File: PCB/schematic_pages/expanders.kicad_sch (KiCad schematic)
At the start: 32 parts

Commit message: repo rearrange
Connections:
- net I2C_SCL renamed I2C_SCK

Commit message: new schematics
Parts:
- removed B24, B25, B26: ~, symbol Symbols:Push_Switch
- added S1, S2, S3: ~, Footprints:MTS-102 Switch, symbol Symbols:Switch
- B1, B11, B12, B13, B14, B15, B16, B17, B18, B19, B2, B20, B21, B22, B23, B3, B4, B5, B6, B7, B8, B9: footprint (none) -> Footprints:Mechanical Switch
- B24: renamed from B27; footprint (none) -> Footprints:Mechanical Switch
- B25: renamed from B28; footprint (none) -> Footprints:Mechanical Switch
- B26: renamed from B29; footprint (none) -> Footprints:Mechanical Switch
- C42, C43: footprint (none) -> Footprints:0603_C
- EX1, EX2: footprint (none) -> Footprints:MCP23017 GPIO Expander
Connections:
- net GND: now also S1.3, S2.3, S3.3
- net at EX2.21 (GPA0): now also S2.2
- net at EX2.22 (GPA1): now also S3.2
- net at EX2.8 (GPB7): now also S1.2
- no-connect marks 0 -> 3

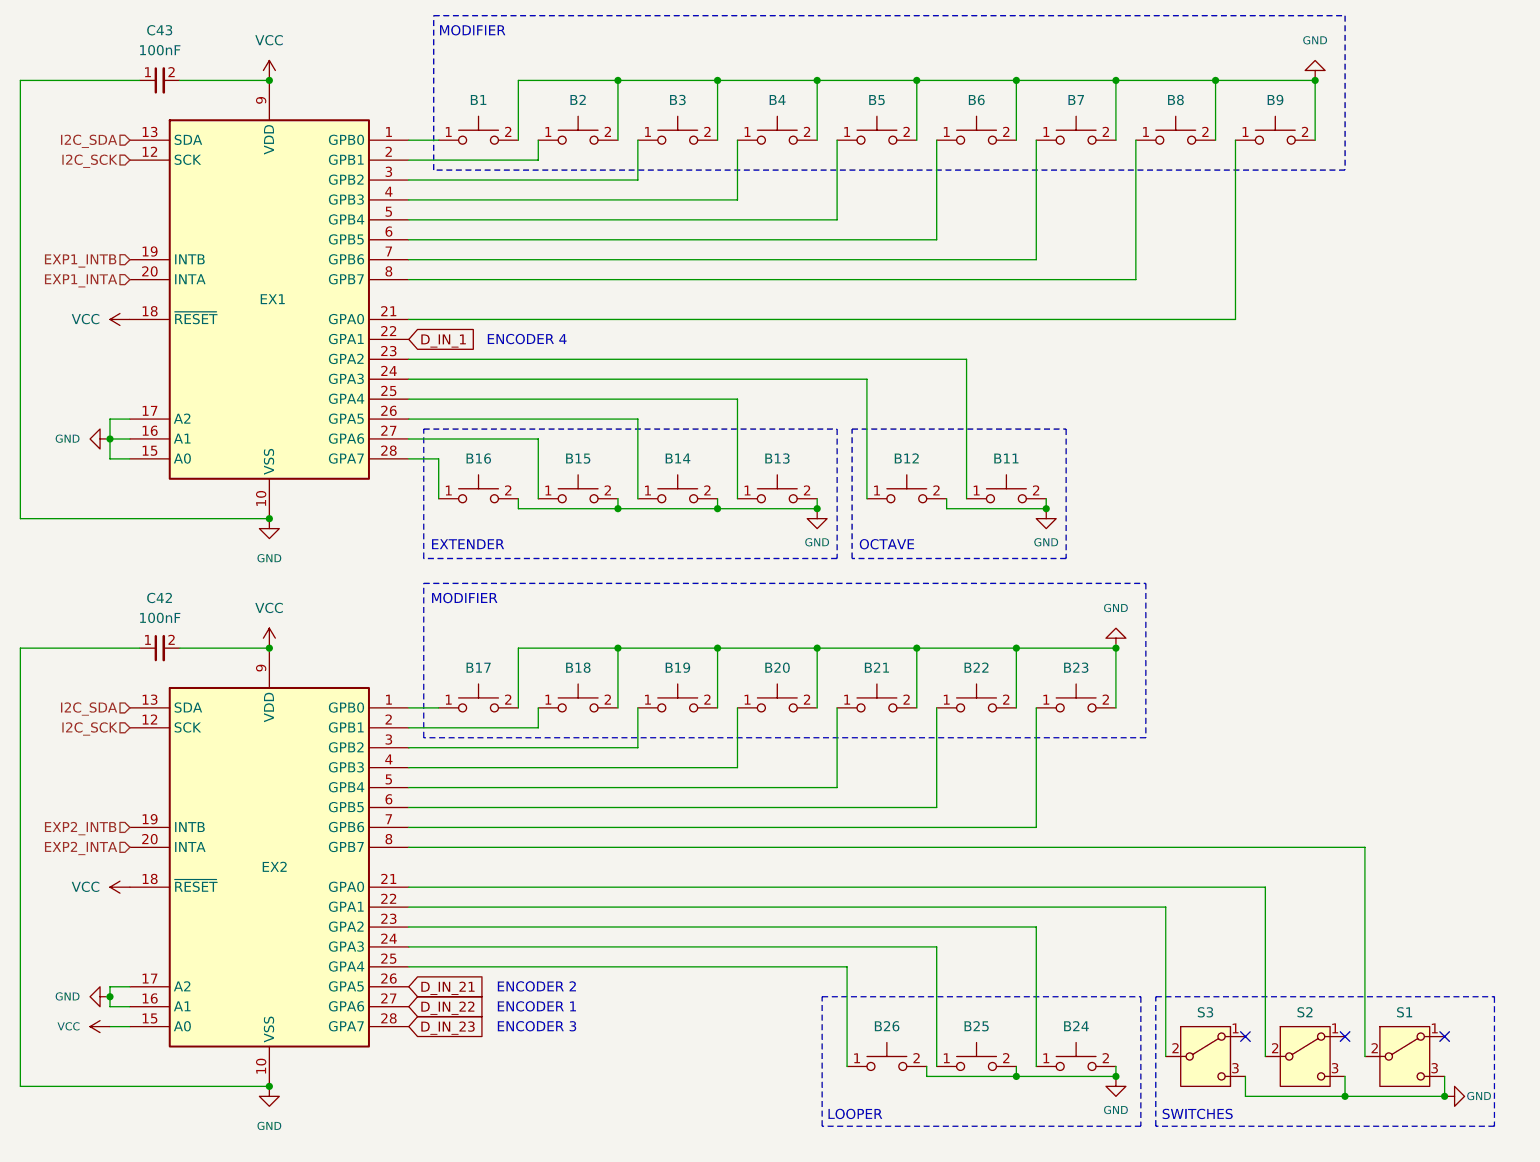
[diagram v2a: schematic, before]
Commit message: ISP ports, RESET lines, MIDI DIN 5
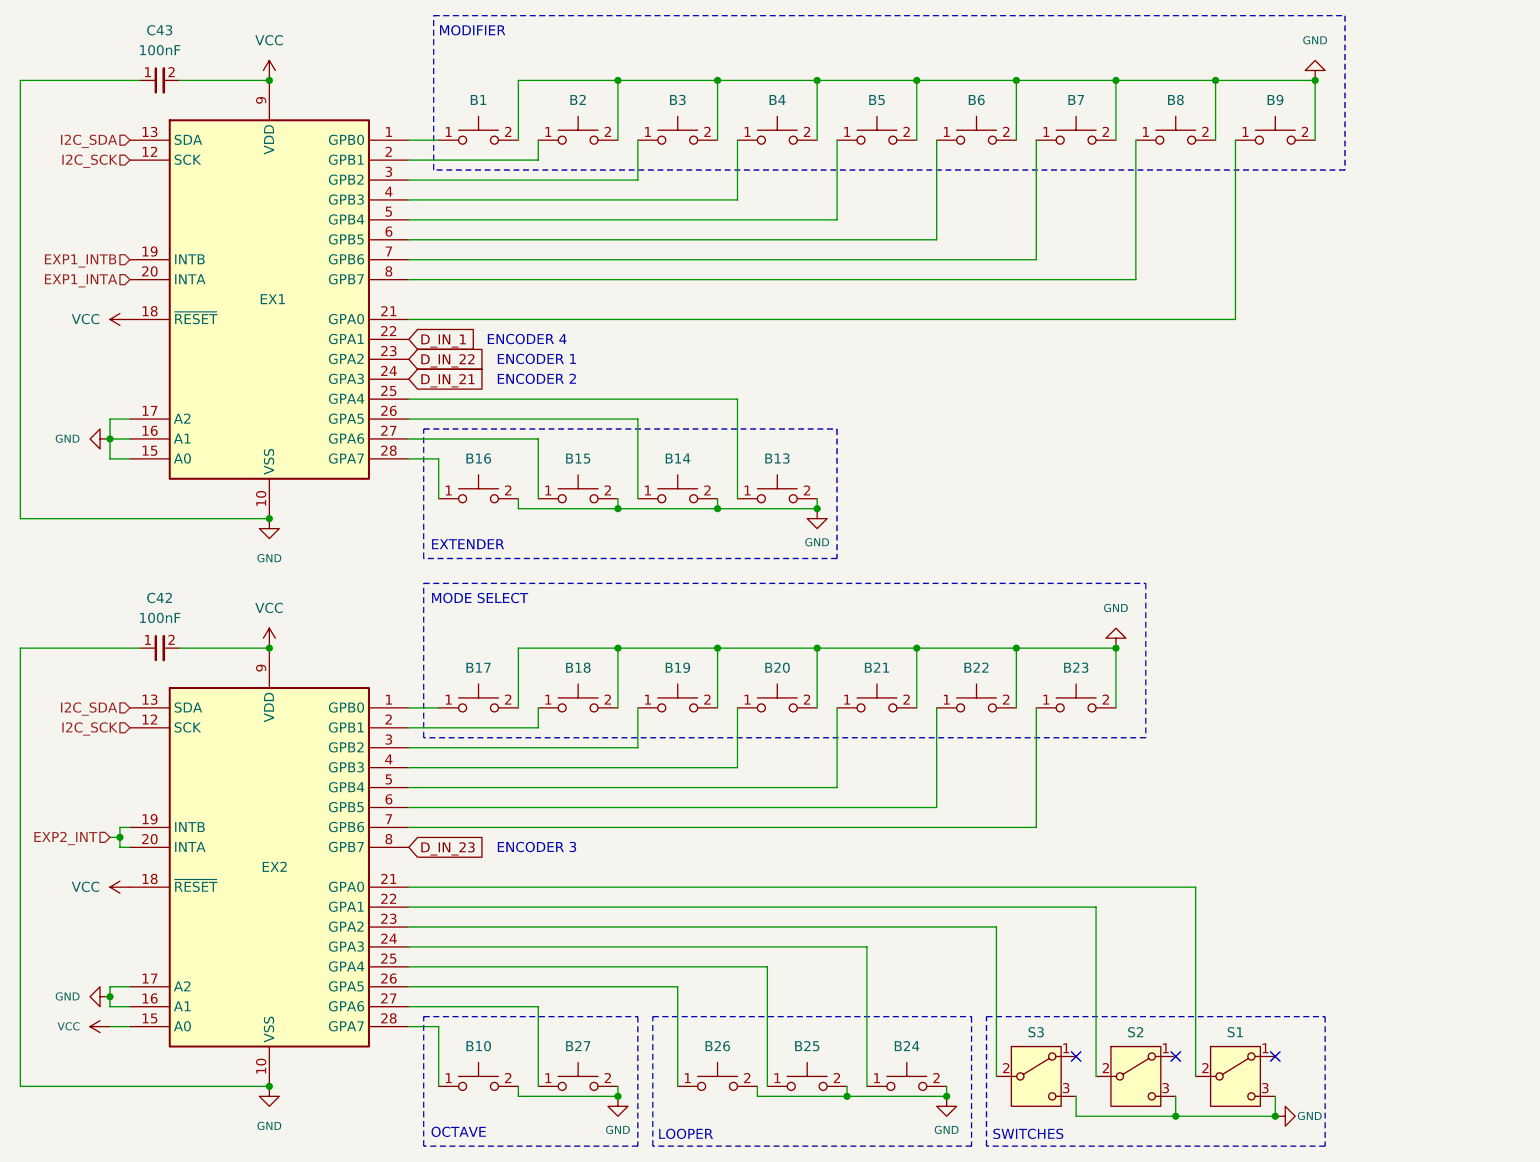
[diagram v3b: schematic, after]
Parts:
- removed B11, B12: ~, Footprints:Mechanical Switch, symbol Symbols:Push_Switch
- added B10, B27: ~, Footprints:Mechanical Switch, symbol Symbols:Push_Switch
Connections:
- net EXP2_INTB is gone; now on net EXP2_INT: EX2.19 (INTB)
- net D_IN_21: now also EX1.24 (GPA3); no longer EX2.26 (GPA5)
- net D_IN_22: now also EX1.23 (GPA2); no longer EX2.27 (GPA6)
- net D_IN_23: now also EX2.8 (GPB7); no longer EX2.28 (GPA7)
- net GND: now also B10.2, B27.2
- net at EX2.21 (GPA0): now also S1.2; no longer S2.2
- net at EX2.22 (GPA1): now also S2.2; no longer S3.2
- net at EX2.23 (GPA2): now also S3.2; no longer B24.1
- net at EX2.24 (GPA3): now also B24.1; no longer B25.1
- net at EX2.25 (GPA4): now also B25.1; no longer B26.1
- net EXP2_INTA renamed EXP2_INT
- new net: B26.1, EX2.26 (GPA5)
- new net: B27.1, EX2.27 (GPA6)
- new net: B10.1, EX2.28 (GPA7)
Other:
- note added: "MODE SELECT"
- moved on the sheet: B24, B25, B26, S1, S2, S3

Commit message: pcbing
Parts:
- renumbered B13 to B10, B14 to B11, B15 to B12, B16 to B13, B17 to B14, B18 to B15, B19 to B16, B20 to B17, B21 to B18, B22 to B19, B23 to B20, B24 to B21, B25 to B22, B26 to B23, B27 to B24, B10 to B25
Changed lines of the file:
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@@
 		(dnp no)
 		(fields_autoplaced yes)
-		(property "Reference" "B17"
+		(property "Reference" "B14"
 			(at 111.76 99.06 0)
 			(effects
@@
 			(project "MCU_328p"
 				(path "/de43e009-b04c-42c1-b131-cdc664039a0d/8f5845f6-f6f8-4f8f-ac6e-d033b6efee1b"
-					(reference "B17")
+					(reference "B14")
 					(unit 1)
 				)
@@
 		(dnp no)
 		(fields_autoplaced yes)
-		(property "Reference" "B25"
+		(property "Reference" "B22"
 			(at 153.67 147.32 0)
 			(effects
@@
 			(project "MCU_328p"
 				(path "/de43e009-b04c-42c1-b131-cdc664039a0d/8f5845f6-f6f8-4f8f-ac6e-d033b6efee1b"
-					(reference "B25")
+					(reference "B22")
 					(unit 1)
 				)
@@
 		(dnp no)
 		(fields_autoplaced yes)
-		(property "Reference" "B18"
+		(property "Reference" "B15"
 			(at 124.46 99.06 0)
 			(effects
@@
 			(project "MCU_328p"
 				(path "/de43e009-b04c-42c1-b131-cdc664039a0d/8f5845f6-f6f8-4f8f-ac6e-d033b6efee1b"
-					(reference "B18")
+					(reference "B15")
 					(unit 1)
 				)
@@
 		(dnp no)
 		(fields_autoplaced yes)
-		(property "Reference" "B10"
+		(property "Reference" "B25"
 			(at 111.76 147.32 0)
 			(effects
@@
 			(project "Harmora"
 				(path "/de43e009-b04c-42c1-b131-cdc664039a0d/8f5845f6-f6f8-4f8f-ac6e-d033b6efee1b"
-					(reference "B10")
+					(reference "B25")
 					(unit 1)
 				)
@@
 		(dnp no)
 		(fields_autoplaced yes)
-		(property "Reference" "B26"
+		(property "Reference" "B23"
 			(at 142.24 147.32 0)
 			(effects
@@
 			(project "MCU_328p"
 				(path "/de43e009-b04c-42c1-b131-cdc664039a0d/8f5845f6-f6f8-4f8f-ac6e-d033b6efee1b"
-					(reference "B26")
+					(reference "B23")
 					(unit 1)
 				)
@@
 		(dnp no)
 		(fields_autoplaced yes)
-		(property "Reference" "B23"
+		(property "Reference" "B20"
 			(at 187.96 99.06 0)
 			(effects
@@
 			(project "MCU_328p"
 				(path "/de43e009-b04c-42c1-b131-cdc664039a0d/8f5845f6-f6f8-4f8f-ac6e-d033b6efee1b"
-					(reference "B23")
+					(reference "B20")
 					(unit 1)
 				)
@@
 		(dnp no)
 		(fields_autoplaced yes)
-		(property "Reference" "B21"
+		(property "Reference" "B18"
 			(at 162.56 99.06 0)
 			(effects
@@
 			(project "MCU_328p"
 				(path "/de43e009-b04c-42c1-b131-cdc664039a0d/8f5845f6-f6f8-4f8f-ac6e-d033b6efee1b"
-					(reference "B21")
+					(reference "B18")
 					(unit 1)
 				)
@@
 		(dnp no)
 		(fields_autoplaced yes)
-		(property "Reference" "B19"
+		(property "Reference" "B16"
 			(at 137.16 99.06 0)
 			(effects
@@
 			(project "MCU_328p"
 				(path "/de43e009-b04c-42c1-b131-cdc664039a0d/8f5845f6-f6f8-4f8f-ac6e-d033b6efee1b"
-					(reference "B19")
+					(reference "B16")
 					(unit 1)
 				)
@@
 		(dnp no)
 		(fields_autoplaced yes)
-		(property "Reference" "B13"
+		(property "Reference" "B10"
 			(at 149.86 72.39 0)
 			(effects
@@
 			(project "MCU_328p"
 				(path "/de43e009-b04c-42c1-b131-cdc664039a0d/8f5845f6-f6f8-4f8f-ac6e-d033b6efee1b"
-					(reference "B13")
+					(reference "B10")
 					(unit 1)
 				)
@@
 		(dnp no)
 		(fields_autoplaced yes)
-		(property "Reference" "B14"
+		(property "Reference" "B11"
 			(at 137.16 72.39 0)
 			(effects
@@
 			(project "MCU_328p"
 				(path "/de43e009-b04c-42c1-b131-cdc664039a0d/8f5845f6-f6f8-4f8f-ac6e-d033b6efee1b"
-					(reference "B14")
+					(reference "B11")
 					(unit 1)
 				)
@@
 		(on_board yes)
 		(dnp no)
-		(property "Reference" "B16"
+		(property "Reference" "B13"
 			(at 111.76 72.39 0)
 			(effects
@@
 			(project "MCU_328p"
 				(path "/de43e009-b04c-42c1-b131-cdc664039a0d/8f5845f6-f6f8-4f8f-ac6e-d033b6efee1b"
-					(reference "B16")
+					(reference "B13")
 					(unit 1)
 				)
@@
 		(dnp no)
 		(fields_autoplaced yes)
-		(property "Reference" "B15"
+		(property "Reference" "B12"
 			(at 124.46 72.39 0)
 			(effects
@@
 			(project "MCU_328p"
 				(path "/de43e009-b04c-42c1-b131-cdc664039a0d/8f5845f6-f6f8-4f8f-ac6e-d033b6efee1b"
-					(reference "B15")
+					(reference "B12")
 					(unit 1)
 				)
@@
 		(dnp no)
 		(fields_autoplaced yes)
-		(property "Reference" "B27"
+		(property "Reference" "B24"
 			(at 124.46 147.32 0)
 			(effects
@@
 			(project "Harmora"
 				(path "/de43e009-b04c-42c1-b131-cdc664039a0d/8f5845f6-f6f8-4f8f-ac6e-d033b6efee1b"
-					(reference "B27")
+					(reference "B24")
 					(unit 1)
 				)
@@
 		(dnp no)
 		(fields_autoplaced yes)
-		(property "Reference" "B20"
+		(property "Reference" "B17"
 			(at 149.86 99.06 0)
 			(effects
@@
 			(project "MCU_328p"
 				(path "/de43e009-b04c-42c1-b131-cdc664039a0d/8f5845f6-f6f8-4f8f-ac6e-d033b6efee1b"
-					(reference "B20")
+					(reference "B17")
 					(unit 1)
 				)
@@
 		(dnp no)
 		(fields_autoplaced yes)
-		(property "Reference" "B24"
+		(property "Reference" "B21"
 			(at 166.37 147.32 0)
 			(effects
@@
 			(project "MCU_328p"
 				(path "/de43e009-b04c-42c1-b131-cdc664039a0d/8f5845f6-f6f8-4f8f-ac6e-d033b6efee1b"
-					(reference "B24")
+					(reference "B21")
 					(unit 1)
 				)
@@
 		(dnp no)
 		(fields_autoplaced yes)
-		(property "Reference" "B22"
+		(property "Reference" "B19"
 			(at 175.26 99.06 0)
 			(effects
@@
 			(project "MCU_328p"
 				(path "/de43e009-b04c-42c1-b131-cdc664039a0d/8f5845f6-f6f8-4f8f-ac6e-d033b6efee1b"
-					(reference "B22")
+					(reference "B19")
 					(unit 1)
 				)

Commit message: longahh day
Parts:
- renumbered B8 to B24, B9 to B25, B25 to B4, B24 to B7, B4 to B8, B7 to B9
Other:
- moved on the sheet: B24, B25
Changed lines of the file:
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@@
 	(paper "A4")
 	(rectangle
+		(start 105.41 143.51)
+		(end 132.715 160.02)
+		(stroke
+			(width 0)
+			(type dash)
+		)
+		(fill
+			(type none)
+		)
+	)
+	(rectangle
 		(start 176.53 143.51)
 		(end 219.71 160.02)
@@
 	(rectangle
 		(start 106.045 15.875)
-		(end 222.25 35.56)
+		(end 195.58 35.56)
 		(stroke
 			(width 0)
@@
 	)
 	(rectangle
-		(start 104.775 143.51)
-		(end 132.08 160.02)
+		(start 197.485 16.51)
+		(end 224.79 34.29)
 		(stroke
 			(width 0)
@@
 		)
 	)
+	(text "MODIFIER"
+		(exclude_from_sim no)
+		(at 106.426 158.242 0)
+		(effects
+			(font
+				(size 1.27 1.27)
+			)
+			(justify left)
+		)
+	)
 	(text "MODE SELECT"
 		(exclude_from_sim no)
@@
 	(text "OCTAVE"
 		(exclude_from_sim no)
-		(at 105.664 158.496 0)
+		(at 198.628 18.542 0)
 		(effects
 			(font
@@
 	)
 	(junction
+		(at 193.04 24.13)
+		(diameter 0)
+		(color 0 0 0 1)
+	)
+	(junction
 		(at 180.34 96.52)
 		(diameter 0)
@@
 	)
 	(junction
-		(at 218.44 24.13)
-		(diameter 0)
-		(color 0 0 0 1)
-	)
-	(junction
-		(at 193.04 24.13)
+		(at 220.98 24.13)
 		(diameter 0)
 		(color 0 0 0 1)
@@
 	)
 	(junction
-		(at 205.74 24.13)
-		(diameter 0)
-		(color 0 0 0 1)
-	)
-	(junction
 		(at 180.34 24.13)
 		(diameter 0)
@@
 	(wire
 		(pts
-			(xy 102.87 49.53) (xy 195.58 49.53)
+			(xy 102.87 49.53) (xy 198.12 49.53)
 		)
 		(stroke
@@
 	(wire
 		(pts
-			(xy 208.28 54.61) (xy 208.28 31.75)
+			(xy 210.82 54.61) (xy 210.82 31.75)
 		)
 		(stroke
@@
 	(wire
 		(pts
-			(xy 205.74 24.13) (xy 205.74 31.75)
+			(xy 208.28 24.13) (xy 208.28 31.75)
 		)
 		(stroke
@@
 	(wire
 		(pts
-			(xy 218.44 24.13) (xy 218.44 31.75)
+			(xy 220.98 24.13) (xy 220.98 31.75)
 		)
 		(stroke
@@
 	(wire
 		(pts
-			(xy 195.58 49.53) (xy 195.58 31.75)
+			(xy 198.12 49.53) (xy 198.12 31.75)
 		)
 		(stroke
@@
 	(wire
 		(pts
-			(xy 205.74 24.13) (xy 218.44 24.13)
+			(xy 208.28 24.13) (xy 220.98 24.13)
 		)
 		(stroke
@@
 	(wire
 		(pts
-			(xy 102.87 54.61) (xy 208.28 54.61)
+			(xy 102.87 54.61) (xy 210.82 54.61)
 		)
 		(stroke
@@
 	(wire
 		(pts
-			(xy 193.04 24.13) (xy 205.74 24.13)
-		)
-		(stroke
-			(width 0)
-			(type default)
-			(color 0 0 0 1)
-		)
-	)
-	(wire
-		(pts
 			(xy 102.87 36.83) (xy 132.08 36.83)
 		)
@@
 	(symbol
 		(lib_id "Symbols:GND")
-		(at 218.44 24.13 180)
+		(at 220.98 24.13 180)
 		(unit 1)
 		(exclude_from_sim no)
@@
 		(fields_autoplaced yes)
 		(property "Reference" "#PWR0106"
-			(at 218.44 24.13 0)
+			(at 220.98 24.13 0)
 			(effects
 				(font
@@
 		)
 		(property "Value" "GND"
-			(at 218.44 19.05 0)
+			(at 220.98 19.05 0)
 			(effects
 				(font
@@
 		)
 		(property "Footprint" ""
-			(at 218.44 24.13 0)
+			(at 220.98 24.13 0)
 			(effects
 				(font
@@
 		)
 		(property "Datasheet" ""
-			(at 218.44 24.13 0)
+			(at 220.98 24.13 0)
 			(effects
 				(font
@@
 		)
 		(property "Description" ""
-			(at 218.44 24.13 0)
+			(at 220.98 24.13 0)
 			(effects
 				(font
@@
 	)
 	(symbol
+		(lib_id "Symbols:GND")
+		(at 193.04 24.13 180)
+		(unit 1)
+		(exclude_from_sim no)
+		(in_bom yes)
+		(on_board yes)
+		(dnp no)
+		(fields_autoplaced yes)
+		(property "Reference" "#PWR0107"
+			(at 193.04 24.13 0)
+			(effects
+				(font
+					(size 1.27 1.27)
+				)
+				(hide yes)
+			)
+		)
+		(property "Value" "GND"
+			(at 193.04 19.05 0)
+			(effects
+				(font
+					(size 1.016 1.016)
+				)
+			)
+		)
+		(property "Footprint" ""
+			(at 193.04 24.13 0)
+			(effects
+				(font
+					(size 1.27 1.27)
+				)
+				(hide yes)
+			)
+		)
+		(property "Datasheet" ""
+			(at 193.04 24.13 0)
+			(effects
+				(font
+					(size 1.27 1.27)
+				)
+				(hide yes)
+			)
+		)
+		(property "Description" ""
+			(at 193.04 24.13 0)
+			(effects
+				(font
+					(size 1.27 1.27)
+				)
+				(hide yes)
+			)
+		)
+		(pin ""
+		)
+		(instances
+			(project "Harmora"
+				(path "/de43e009-b04c-42c1-b131-cdc664039a0d/8f5845f6-f6f8-4f8f-ac6e-d033b6efee1b"
+					(reference "#PWR0107")
+					(unit 1)
+				)
+			)
+		)
+	)
+	(symbol
 		(lib_id "power:VCC")
 		(at 67.31 127 90)
@@
 		(dnp no)
 		(fields_autoplaced yes)
-		(property "Reference" "B25"
+		(property "Reference" "B4"
 			(at 111.76 147.32 0)
 			(effects
@@
 			(project "Harmora"
 				(path "/de43e009-b04c-42c1-b131-cdc664039a0d/8f5845f6-f6f8-4f8f-ac6e-d033b6efee1b"
-					(reference "B25")
+					(reference "B4")
 					(unit 1)
 				)
@@
 		(dnp no)
 		(fields_autoplaced yes)
-		(property "Reference" "B7"
+		(property "Reference" "B9"
 			(at 187.96 26.67 0)
 			(effects
@@
 			(project "MCU_328p"
 				(path "/de43e009-b04c-42c1-b131-cdc664039a0d/8f5845f6-f6f8-4f8f-ac6e-d033b6efee1b"
-					(reference "B7")
+					(reference "B9")
 					(unit 1)
 				)
@@
 	(symbol
 		(lib_id "Symbols:Push_Switch")
-		(at 213.36 31.75 0)
+		(at 215.9 31.75 0)
 		(unit 1)
 		(exclude_from_sim no)
@@
 		(dnp no)
 		(fields_autoplaced yes)
-		(property "Reference" "B9"
-			(at 213.36 26.67 0)
+		(property "Reference" "B25"
+			(at 215.9 26.67 0)
 			(effects
 				(font
@@
 		)
 		(property "Value" "~"
-			(at 213.36 31.75 0)
+			(at 215.9 31.75 0)
 			(effects
 				(font
@@
 		)
 		(property "Footprint" "Footprints:Mechanical Switch"
-			(at 213.36 31.75 0)
+			(at 215.9 31.75 0)
 			(effects
 				(font
@@
 		)
 		(property "Datasheet" ""
-			(at 213.36 31.75 0)
+			(at 215.9 31.75 0)
 			(effects
 				(font
@@
 		)
 		(property "Description" ""
-			(at 213.36 31.75 0)
+			(at 215.9 31.75 0)
 			(effects
 				(font
@@
 			(project "MCU_328p"
 				(path "/de43e009-b04c-42c1-b131-cdc664039a0d/8f5845f6-f6f8-4f8f-ac6e-d033b6efee1b"
-					(reference "B9")
+					(reference "B25")
 					(unit 1)
 				)
@@
 		(dnp no)
 		(fields_autoplaced yes)
-		(property "Reference" "B4"
+		(property "Reference" "B8"
 			(at 149.86 26.67 0)
 			(effects
@@
 			(project "MCU_328p"
 				(path "/de43e009-b04c-42c1-b131-cdc664039a0d/8f5845f6-f6f8-4f8f-ac6e-d033b6efee1b"
-					(reference "B4")
+					(reference "B8")
 					(unit 1)
 				)
@@
 		(dnp no)
 		(fields_autoplaced yes)
-		(property "Reference" "B24"
+		(property "Reference" "B7"
 			(at 124.46 147.32 0)
 			(effects
@@
 			(project "Harmora"
 				(path "/de43e009-b04c-42c1-b131-cdc664039a0d/8f5845f6-f6f8-4f8f-ac6e-d033b6efee1b"
-					(reference "B24")
+					(reference "B7")
 					(unit 1)
 				)
@@
 	(symbol
 		(lib_id "Symbols:Push_Switch")
-		(at 200.66 31.75 0)
+		(at 203.2 31.75 0)
 		(unit 1)
 		(exclude_from_sim no)
@@
 		(dnp no)
 		(fields_autoplaced yes)
-		(property "Reference" "B8"
-			(at 200.66 26.67 0)
+		(property "Reference" "B24"
+			(at 203.2 26.67 0)
 			(effects
 				(font
@@
 		)
 		(property "Value" "~"
-			(at 200.66 31.75 0)
+			(at 203.2 31.75 0)
 			(effects
 				(font
@@
 		)
 		(property "Footprint" "Footprints:Mechanical Switch"
-			(at 200.66 31.75 0)
+			(at 203.2 31.75 0)
 			(effects
 				(font
@@
 		)
 		(property "Datasheet" ""
-			(at 200.66 31.75 0)
+			(at 203.2 31.75 0)
 			(effects
 				(font
@@
 		)
 		(property "Description" ""
-			(at 200.66 31.75 0)
+			(at 203.2 31.75 0)
 			(effects
 				(font
@@
 			(project "MCU_328p"
 				(path "/de43e009-b04c-42c1-b131-cdc664039a0d/8f5845f6-f6f8-4f8f-ac6e-d033b6efee1b"
-					(reference "B8")
+					(reference "B24")
 					(unit 1)
 				)
